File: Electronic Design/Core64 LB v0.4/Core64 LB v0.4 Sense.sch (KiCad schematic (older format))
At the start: 18 parts, among them J6 Conn_01x08_Female, U3 LM393, U5 74HC02, U7 LM393

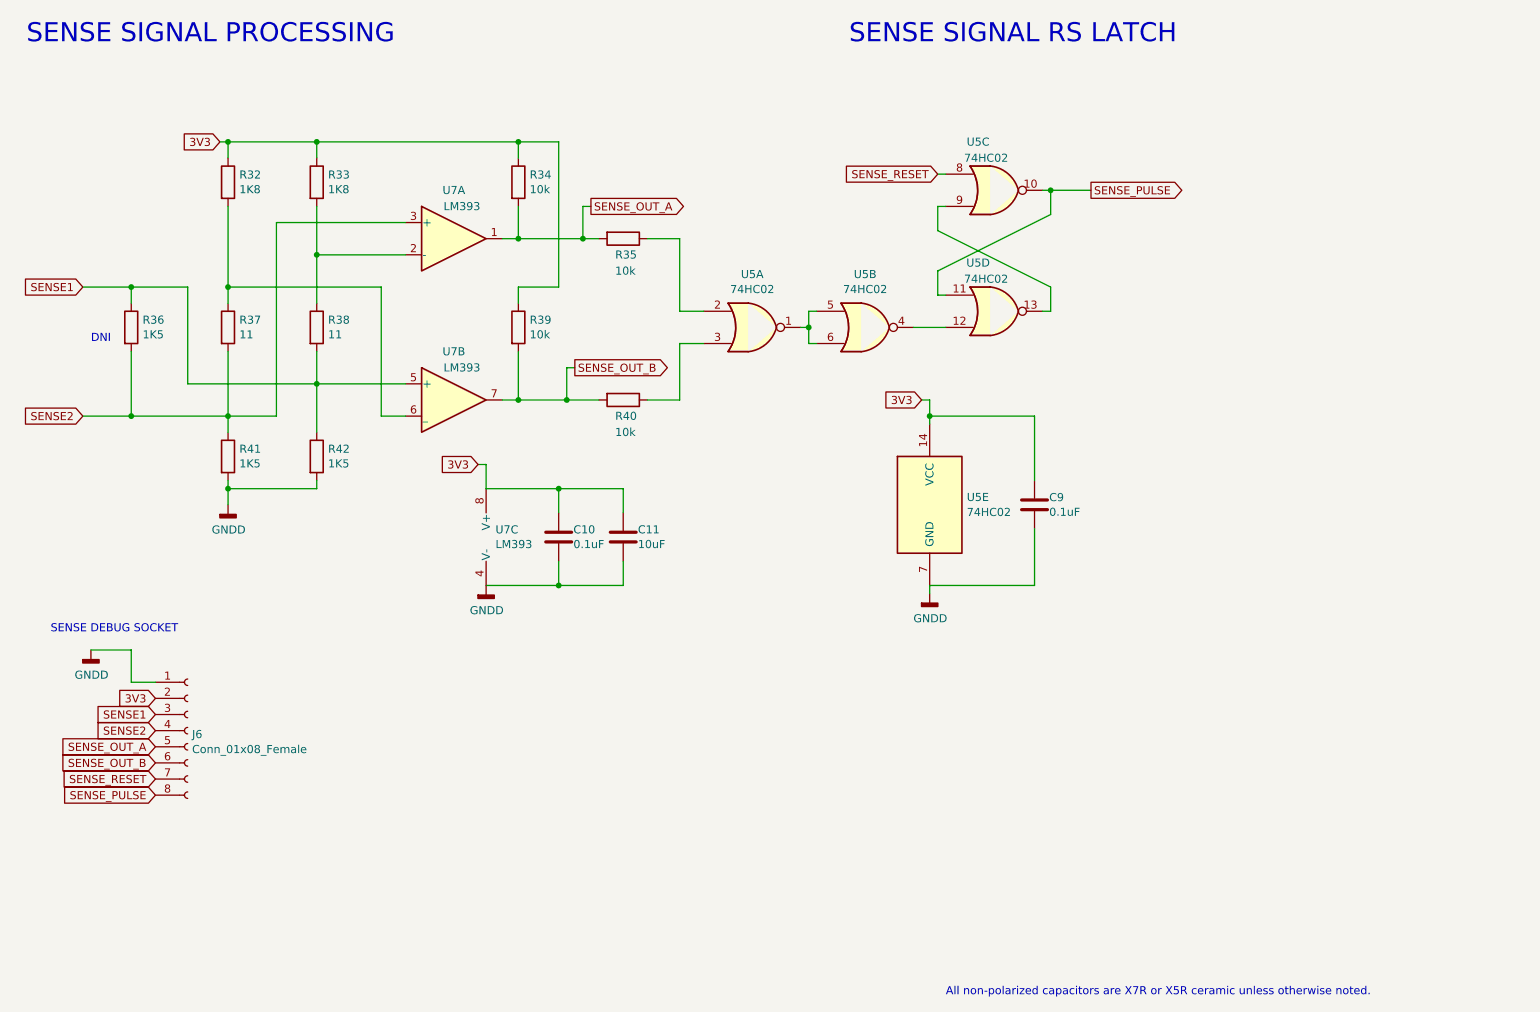
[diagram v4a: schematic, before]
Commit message: Add 3-to-8 and begin other expansion on schematic
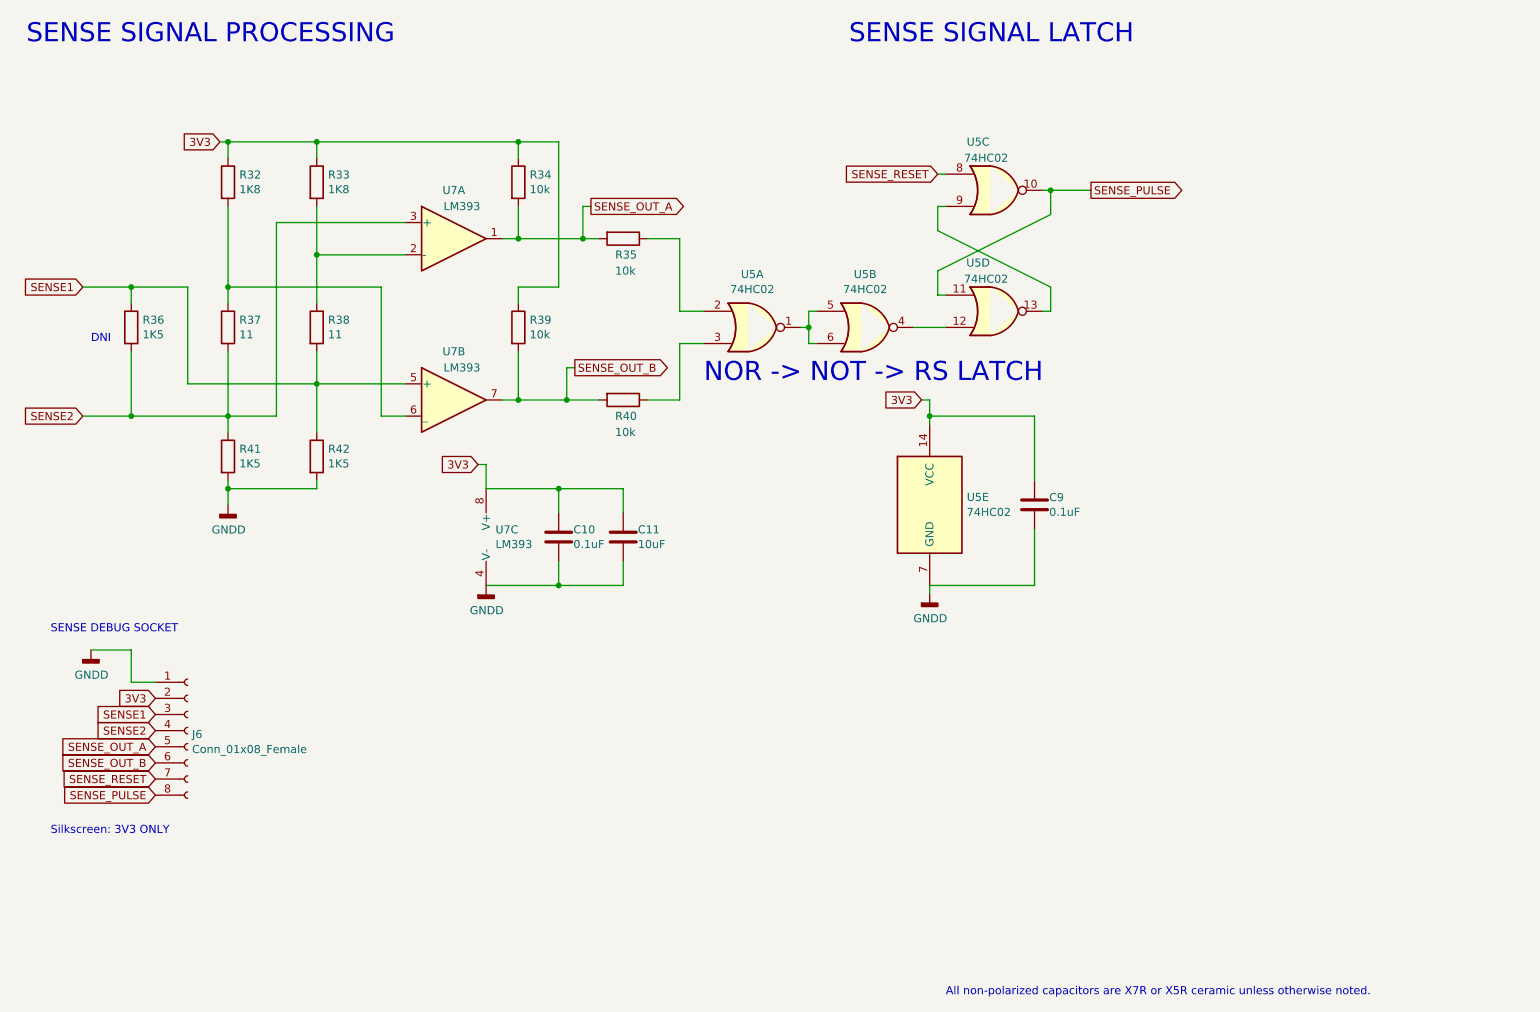
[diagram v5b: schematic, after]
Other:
- note added: "NOR -> NOT -> RS LATCH"
- note added: "SENSE SIGNAL LATCH"
- note added: "Silkscreen: 3V3 ONLY"
- note removed: "SENSE SIGNAL RS LATCH"
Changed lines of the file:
@@
 	3900 4200 4300 4200
 Text Notes 5700 850  0    118  ~ 0
-SENSE SIGNAL RS LATCH
+SENSE SIGNAL LATCH
 Text GLabel 7200 1750 2    50   Output ~ 0
 SENSE_PULSE
@@
 Text Notes 6300 6750 0    50   ~ 0
 All non-polarized capacitors are X7R or X5R ceramic unless otherwise noted.
+Text Notes 750  5750 0    50   ~ 0
+Silkscreen: 3V3 ONLY
+Text Notes 4800 2950 0    118  ~ 0
+NOR -> NOT -> RS LATCH
 $EndSCHEMATC

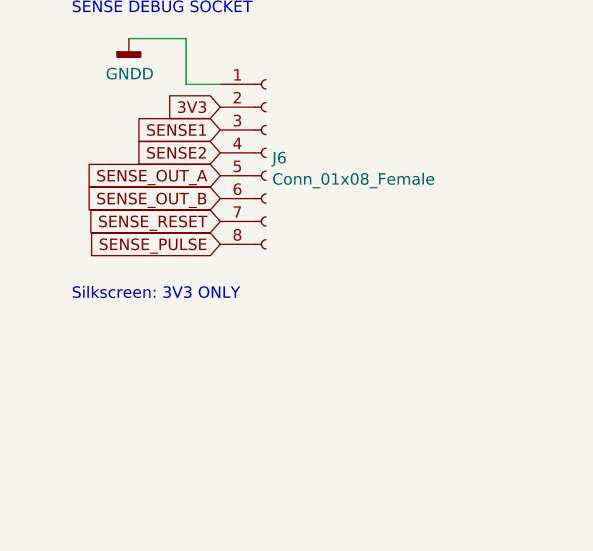
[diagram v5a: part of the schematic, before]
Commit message: Update schematic and XLS pin usage
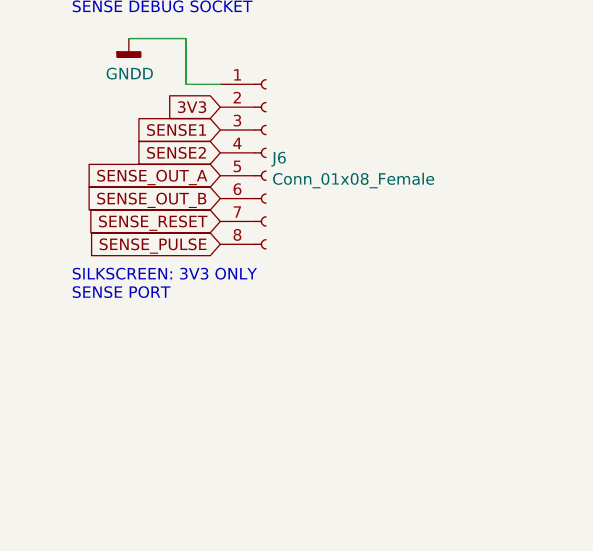
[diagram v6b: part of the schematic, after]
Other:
- note added: "SILKSCREEN: 3V3 ONLY\nSENSE PORT"
- note removed: "Silkscreen: 3V3 ONLY"
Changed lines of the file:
@@
 All non-polarized capacitors are X7R or X5R ceramic unless otherwise noted.
 Text Notes 750  5750 0    50   ~ 0
-Silkscreen: 3V3 ONLY
+SILKSCREEN: 3V3 ONLY\nSENSE PORT
 Text Notes 4800 2950 0    118  ~ 0
 NOR -> NOT -> RS LATCH

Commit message: Update schematic
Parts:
- J6: symbol Connector:Conn_01x08_Female -> Connector_Generic:Conn_01x08
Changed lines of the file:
@@
 	2400 1450 1850 1450
 $Comp
-L Connector:Conn_01x08_Female J6
+L Connector_Generic:Conn_01x08 J6
 U 1 1 5E868B9C
 P 1600 5100
